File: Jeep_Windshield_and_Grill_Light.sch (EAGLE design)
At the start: 15 parts, among them K1 CM1A-P-12V, K2 CM1A-P-12V

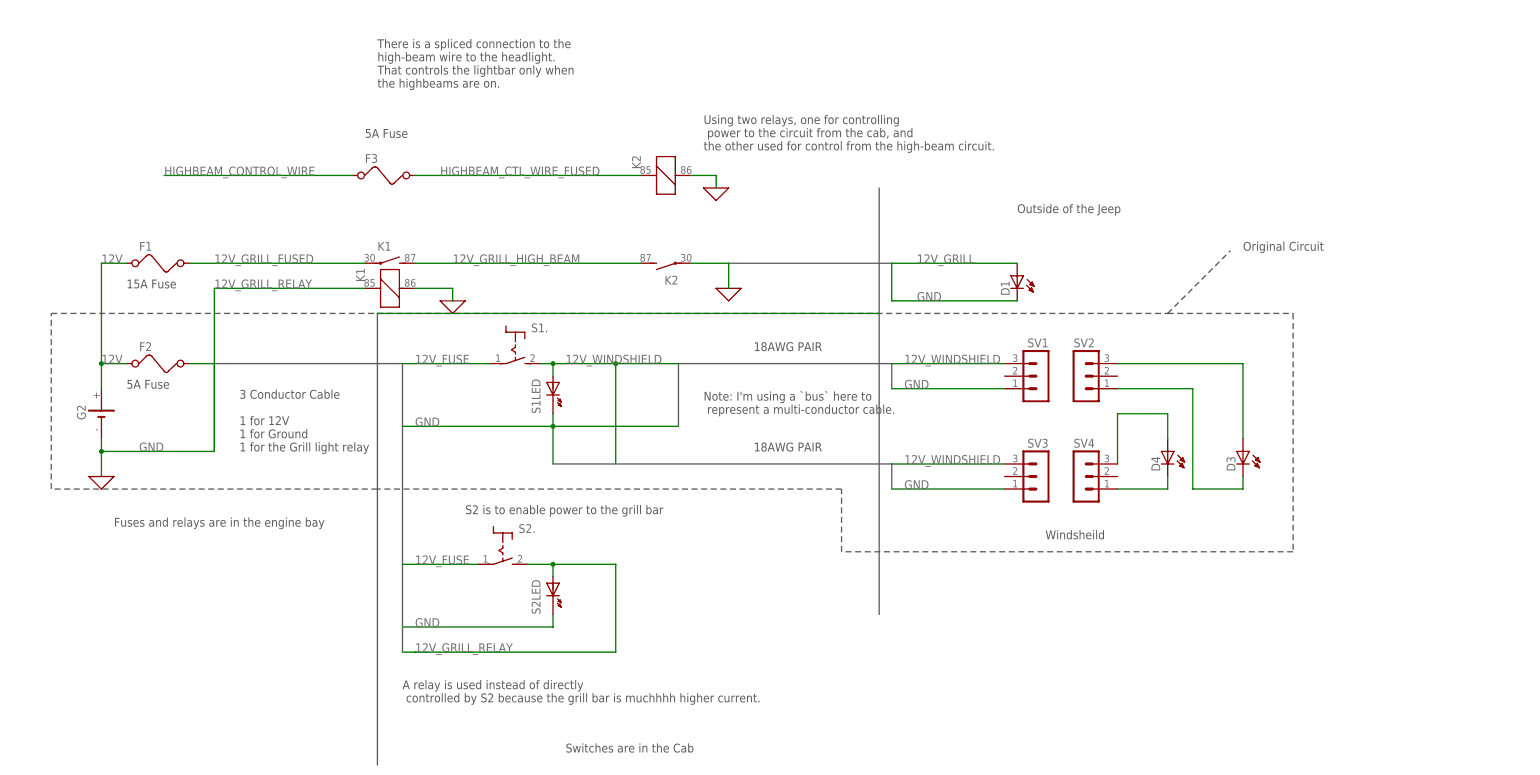
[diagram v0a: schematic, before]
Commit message: Updating grill version to include the ignition wiring. Also updating the original version to look consistent.
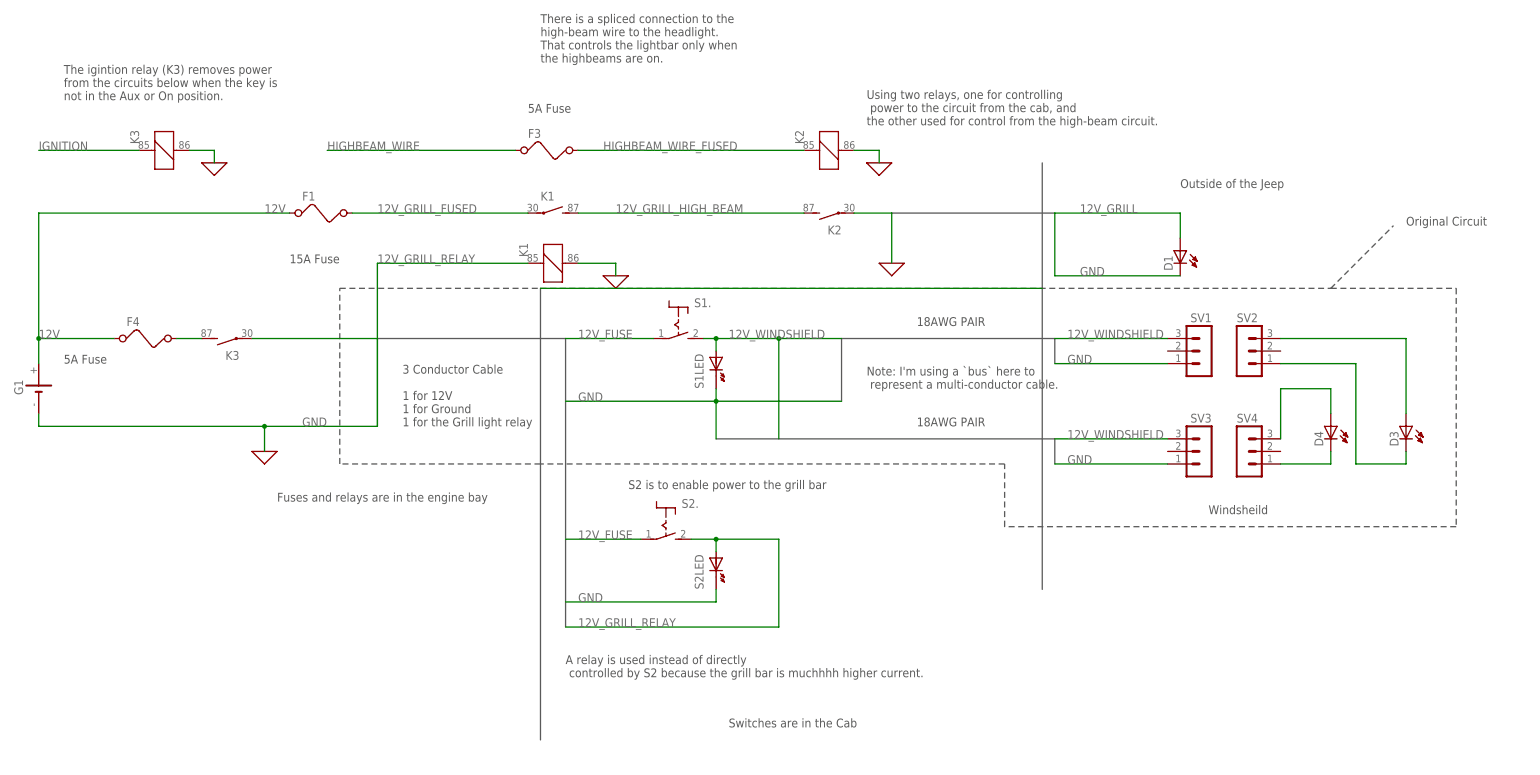
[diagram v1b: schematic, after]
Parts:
- removed F2: (no value), special:FUSE
- removed G2: SL340B, battery:SL340B
- added F4: (no value), special:FUSE
- added G1: SL340B, battery:SL340B
- added K3: CM1A-P-12V, relay:CM1A-P-12V
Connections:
- net HIGHBEAM_CONTROL_WIRE renamed HIGHBEAM_WIRE
- net HIGHBEAM_CTL_WIRE_FUSED renamed HIGHBEAM_WIRE_FUSED
- new net IGNITION: K31.1
- new net N$6: F4.2, K32.S
- net 0: now also K31.2
- net 12V: now also F4.1, G1.+; no longer F2.1, G2.+
- net 12V_FUSE: now also K32.P; no longer F2.2
- net GND: now also G1.-, S1LED.K; no longer G2.-
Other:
- note added: "The igintion relay (K3) removes power from the circuits below when the key is not in the Aux or On position."
- moved on the sheet: D1, D3, D4, F1, F3, K1, K2, S1., S1LED, S2., S2LED, SV1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
